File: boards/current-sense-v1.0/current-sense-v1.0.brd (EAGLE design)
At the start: 71.5 x 95.6 mm, 90 parts, among them IC1 ISO7241, IC2 ISO7241, IC3 ISO7242, IC4 ISO7240, J1 4-PIN_2MM-H, J2 MKS-1658, J3 8-PIN_2MM-H, J6 DF22-2, Q1 IRFH7545, Q2 IRFH7545, Q3 IRFH7545, Q4 IRFH7545, Q5 IRFH7545, Q6 IRFH7545, U1 DRV8303DCA, U13 TLV70233DBVR, U2 INA240PWR, U3 INA240PWR, U4 INA240PWR, U5 TLV70233DBVR, U6 ADS8028IRTJT, U7 MPM3620GQV-P, U8 VND5E006ASPTR-E, U9 TLV70450

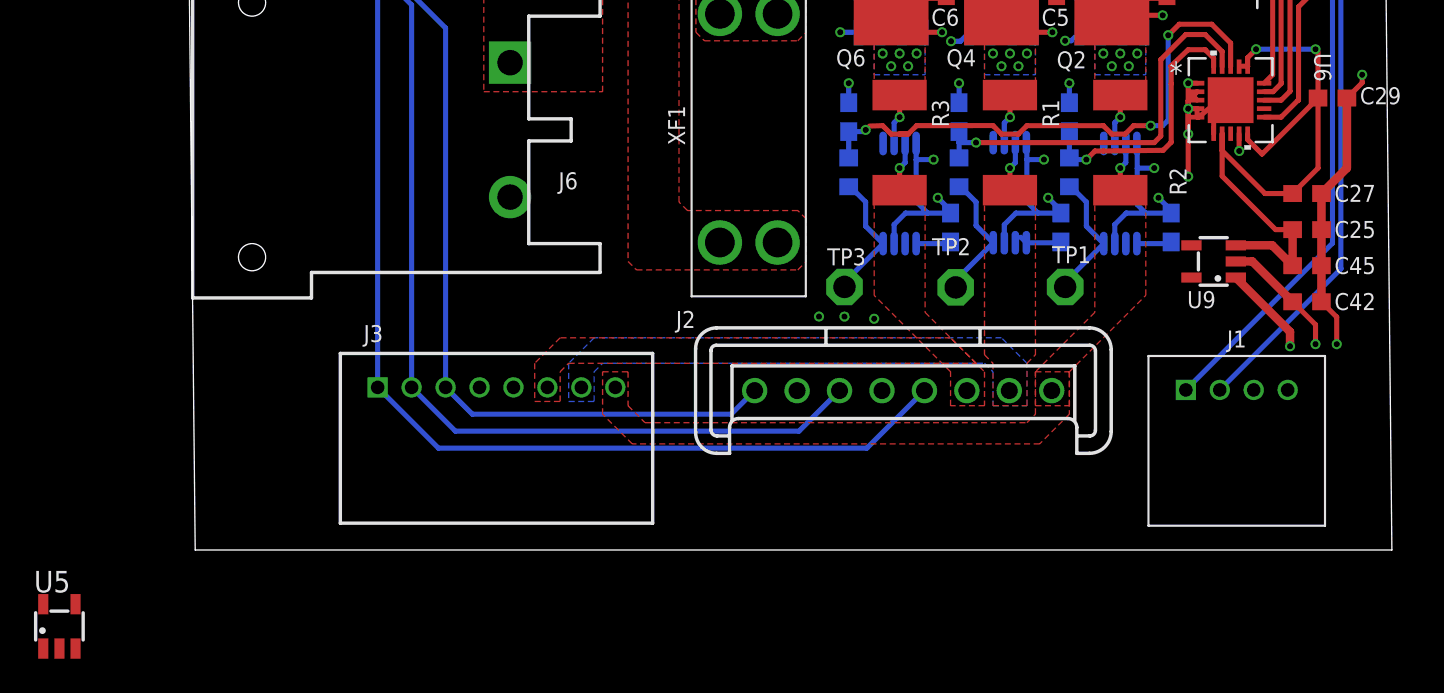
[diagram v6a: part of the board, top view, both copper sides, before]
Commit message: replaced TLV 70450 with TLV 70433
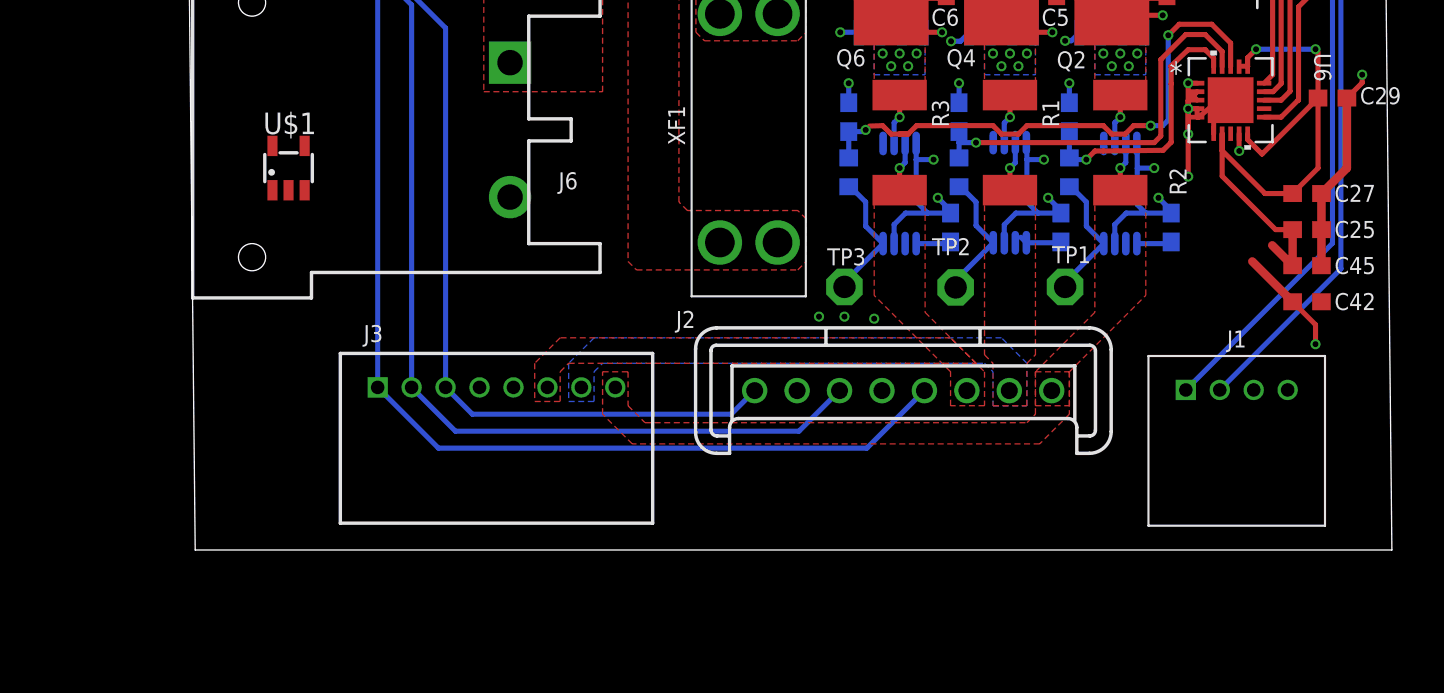
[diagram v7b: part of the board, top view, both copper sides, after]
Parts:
- removed U5: TLV70233DBVR, RoboJackets-PowerICs:SOT-23-5
- removed U9: TLV70450, RoboJackets-PowerICs:SOT-23-5
- added U$1: TLV70433, RoboJackets-PowerICs:SOT-23-5
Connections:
- net +18.5V: no longer U9.2
- net ADC_3V3: no longer U9.3
- net GND: now also U$1.1; no longer U9.1
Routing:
- net GND: track 197.9 -> 187.5 mm, vias 68 -> 66
- net ADC_3V3: track 40.8 -> 38.6 mm
- net +18.5V: track 21.2 -> 20.2 mm

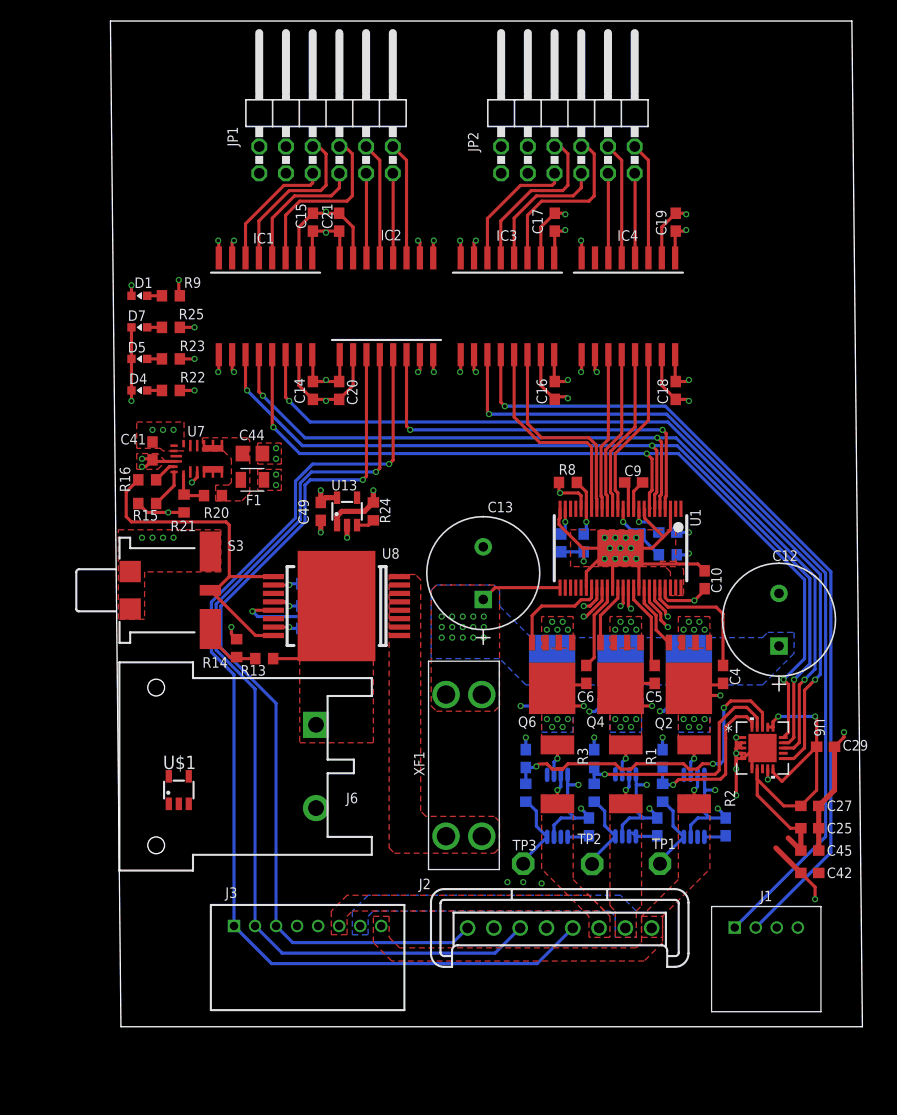
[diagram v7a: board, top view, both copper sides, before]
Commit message: Fixed board dimensions and some other borders
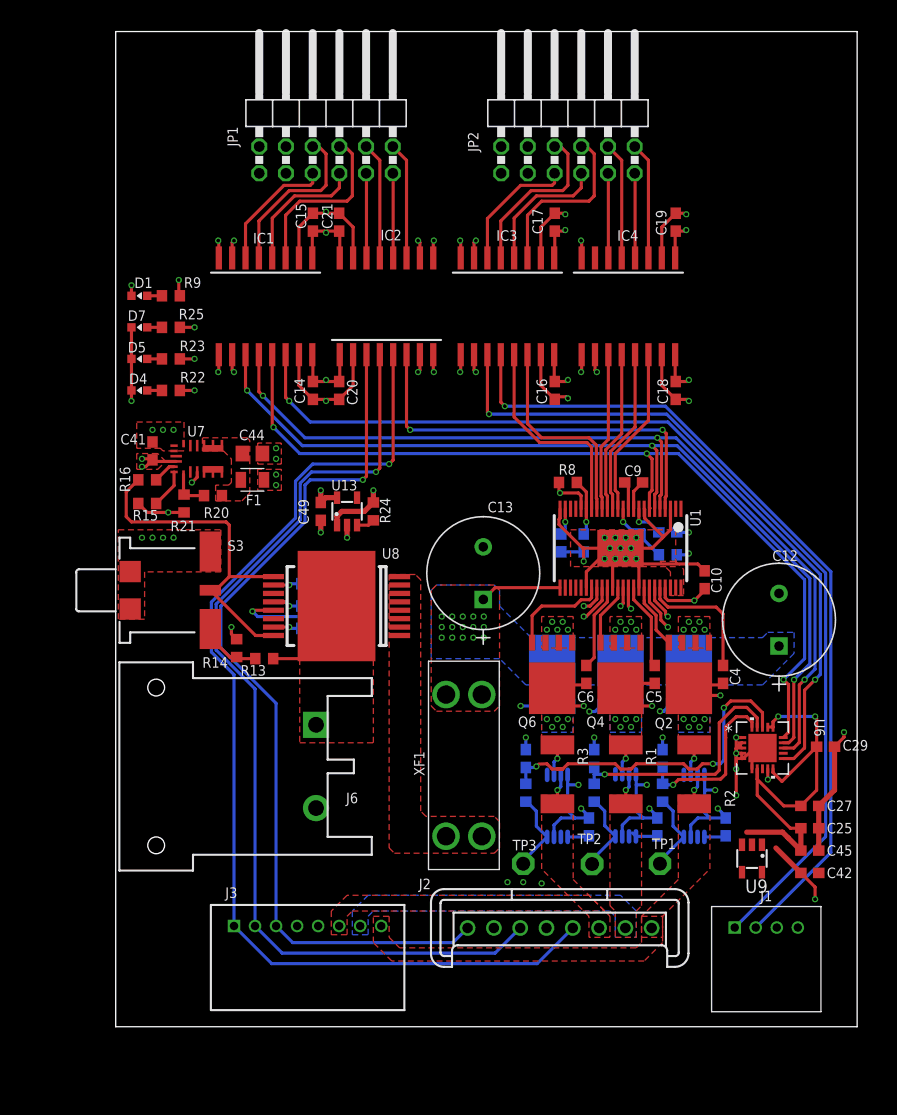
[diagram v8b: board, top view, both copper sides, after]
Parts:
- removed U$1: TLV70433, RoboJackets-PowerICs:SOT-23-5
- added U9: TLV70433, RoboJackets-PowerICs:SOT-23-5
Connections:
- net GND: now also U9.1; no longer U$1.1
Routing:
- net ADC_3V3: track 38.6 -> 42.8 mm
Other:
- board size 71.5 x 95.6 mm -> 70.5 x 94.6 mm
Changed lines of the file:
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@@
 <board>
 <plain>
-<wire x1="0.5" y1="-5" x2="71" y2="-5" width="0" layer="20"/>
-<wire x1="71" y1="-5" x2="70" y2="90.625" width="0" layer="20"/>
-<wire x1="70" y1="90.625" x2="-0.5" y2="90.625" width="0" layer="20"/>
-<wire x1="-0.5" y1="90.625" x2="0.5" y2="-5" width="0" layer="20"/>
+<wire x1="0" y1="-5" x2="70.5" y2="-5" width="0" layer="20"/>
+<wire x1="70.5" y1="-5" x2="70.5" y2="89.625" width="0" layer="20"/>
+<wire x1="70.5" y1="89.625" x2="0" y2="89.625" width="0" layer="20"/>
+<wire x1="0" y1="89.625" x2="0" y2="-5" width="0" layer="20"/>
 </plain>
 <attributes>
@@
 <attribute name="VALUE" x="2.885" y="66.405" size="1.27" layer="27" rot="R180"/>
 </element>
-<element name="U$1" library="RoboJackets-PowerICs" package="SOT-23-5" value="TLV70433" x="6" y="17.5" smashed="yes">
-<attribute name="NAME" x="4.5" y="19.5" size="1.27" layer="25" ratio="10"/>
+<element name="U9" library="RoboJackets-PowerICs" package="SOT-23-5" value="TLV70433" x="60.5" y="11" smashed="yes" rot="R180">
+<attribute name="NAME" x="62" y="9" size="1.27" layer="25" ratio="10" rot="R180"/>
 </element>
 </elements>
@@
 <wire x1="59.525" y1="21" x2="59.525" y2="20.5" width="0.3" layer="1"/>
 <contactref element="C42" pad="2"/>
-<contactref element="U$1" pad="1"/>
+<contactref element="U9" pad="1"/>
 <wire x1="44.305" y1="58.9" x2="51.925" y2="58.9" width="0" layer="19" extent="1-1"/>
 <wire x1="43" y1="54.75" x2="44.25" y2="57.25" width="0" layer="19" extent="1-1"/>
@@
 <wire x1="62.5" y1="22" x2="61.456621875" y2="22.043378125" width="0" layer="19" extent="1-1"/>
 <wire x1="62.000125" y1="19.525" x2="60.499746875" y2="19.525" width="0" layer="19" extent="1-1"/>
+<wire x1="61.45" y1="12.306" x2="59" y2="17" width="0" layer="19" extent="1-1"/>
 <wire x1="39" y1="21.35" x2="42.975003125" y2="18.950003125" width="0" layer="19" extent="16-16"/>
 <wire x1="66.85" y1="16" x2="62.0074125" y2="18.5074125" width="0" layer="19" extent="1-1"/>
@@
 <wire x1="19.05" y1="15.79" x2="19.35" y2="32.875" width="0" layer="19" extent="16-16"/>
 <wire x1="17.25" y1="4.58" x2="19.05" y2="15.79" width="0" layer="19" extent="1-1"/>
-<wire x1="5.05" y1="16.194" x2="17.25" y2="4.58" width="0" layer="19" extent="1-1"/>
 </signal>
 <signal name="PHASE_A">
@@
 <via x="6" y="66" extent="1-16" drill="0.35"/>
 <polygon width="0.3" layer="3" thermals="no">
-<vertex x="0" y="90.625"/>
+<vertex x="0" y="89.125"/>
 <vertex x="0" y="64.5"/>
 <vertex x="70.5" y="64.5"/>
-<vertex x="70.5" y="90.625"/>
+<vertex x="70.5" y="89.125"/>
 </polygon>
 <wire x1="11.075" y1="68.1" x2="11.075" y2="69.575" width="0.3" layer="1"/>
@@
 <via x="1.5" y="65.5" extent="1-16" drill="0.35"/>
 <polygon width="0.3" layer="2" thermals="no">
-<vertex x="0" y="90.875"/>
+<vertex x="0" y="89.375"/>
 <vertex x="0" y="64.5"/>
 <vertex x="70.5" y="64.5"/>
-<vertex x="70.5" y="90.875"/>
+<vertex x="70.5" y="89.375"/>
 </polygon>
 <wire x1="9.805" y1="68.1" x2="9.805" y2="69.695" width="0.3" layer="1"/>
@@
 <via x="63" y="24.5" extent="1-16" drill="0.35"/>
 <wire x1="63" y1="24.5" x2="66.5" y2="24.5" width="0.3" layer="16"/>
+<wire x1="63.95" y1="12.95" x2="63.4" y2="13.5" width="0.5" layer="1"/>
+<wire x1="63.4" y1="13.5" x2="60" y2="13.5" width="0.5" layer="1"/>
 </signal>
 <signal name="OUT_A">
